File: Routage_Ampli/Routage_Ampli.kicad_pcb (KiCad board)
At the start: 2 copper layers, 3 parts

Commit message: Début Placement + Routage
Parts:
- removed REF**: PhoenixContact_MSTBVA_2,5_2-G-5,08_1x02_P5.08mm_Vertical, Connector_Phoenix_MSTB:PhoenixContact_MSTBVA_2,5_2-G-5,08_1x02_P5.08mm_Vertical
- removed REF**: PhoenixContact_MSTBVA_2,5_3-G-5,08_1x03_P5.08mm_Vertical, Connector_Phoenix_MSTB:PhoenixContact_MSTBVA_2,5_3-G-5,08_1x03_P5.08mm_Vertical
- removed REF**: Jack_35RAPC2AV, Routage_Ampli:Jack_35RAPC2AV
- added C1: 47µ, CmpAmpliAudio:CP_Radial_D8.0mm_P5.00mm, F.Cu at (110.5, 125.7)
- added C10: 470µ, CmpAmpliAudio:CP_Radial_D12.5mm_P5.00mm, F.Cu at (176.5, 61.0)
- added C11: 100n, CmpAmpliAudio:C_Rect_L7.2mm_W3.5mm_P5.00mm_FKS2_FKP2_MKS2_MKP2, F.Cu at (170.2, 49.5)
- added C2: C, CmpAmpliAudio:C_Rect_L7.2mm_W3.5mm_P5.00mm_FKS2_FKP2_MKS2_MKP2, F.Cu at (142.2, 99.1)
- added C3: 47µ, CmpAmpliAudio:CP_Radial_D8.0mm_P5.00mm, F.Cu at (152.4, 62.2)
- added C4: 10µ, CmpAmpliAudio:CP_Radial_D8.0mm_P5.00mm, F.Cu at (114.3, 57.1)
- added C5: 100n, CmpAmpliAudio:C_Rect_L7.2mm_W3.5mm_P5.00mm_FKS2_FKP2_MKS2_MKP2, F.Cu at (110.5, 68.6)
- added C6: 10µ, CmpAmpliAudio:CP_Radial_D8.0mm_P5.00mm, F.Cu at (157.5, 49.5)
- added C7: 100n, CmpAmpliAudio:C_Rect_L7.2mm_W3.5mm_P5.00mm_FKS2_FKP2_MKS2_MKP2, F.Cu at (146.1, 49.5)
- added C8: 470µ, CmpAmpliAudio:CP_Radial_D12.5mm_P5.00mm, F.Cu at (190.5, 71.1)
- added C9: 100n, CmpAmpliAudio:C_Rect_L7.2mm_W3.5mm_P5.00mm_FKS2_FKP2_MKS2_MKP2, F.Cu at (199.4, 64.8)
- added D1: 1N4148, CmpAmpliAudio:D_DO-35_SOD27_P10.16mm_Horizontal, F.Cu at (199.4, 69.8)
- added D2: 1N4148, CmpAmpliAudio:D_DO-35_SOD27_P10.16mm_Horizontal, F.Cu at (147.3, 61.0)
- added Dz1: BZX55C5V1, CmpAmpliAudio:D_DO-35_SOD27_P10.16mm_Horizontal, F.Cu at (138.4, 83.8)
- added HS1: Heatsink, CmpAmpliAudio:Heatsink_Fischer_SK104-STC-STIC_35x13mm_2xDrill2.5mm, F.Cu at (165.7, 130.8)
- added HS2: Heatsink, CmpAmpliAudio:Heatsink_Fischer_SK104-STC-STIC_35x13mm_2xDrill2.5mm, F.Cu at (137.8, 74.3)
- added J1: Conn_01x03, CmpAmpliAudio:PhoenixContact_MSTBVA_2,5_3-G-5,08_1x03_P5.08mm_Vertical, F.Cu at (133.3, 52.1)
- added J2: Conn_01x02, CmpAmpliAudio:PhoenixContact_MSTBVA_2,5_2-G-5,08_1x02_P5.08mm_Vertical, F.Cu at (186.7, 54.6)
- added Q1: 2N2907, CmpAmpliAudio:TO-18-3, F.Cu at (125.7, 109.2)
- added Q10: TIP32, CmpAmpliAudio:TO-220-3_Vertical, F.Cu at (140.3, 69.2)
- added Q11: BD138, CmpAmpliAudio:TO-126-3_Vertical, F.Cu at (168.9, 114.3)
- added Q12: TIP31, CmpAmpliAudio:TO-220-3_Vertical, F.Cu at (168.9, 125.7)
- added Q13: 2N2222, CmpAmpliAudio:TO-18-3, F.Cu at (185.4, 96.5)
- added Q2: 2N2907, CmpAmpliAudio:TO-18-3, F.Cu at (160.0, 109.2)
- added Q3: 2N2907, CmpAmpliAudio:TO-18-3, F.Cu at (115.6, 105.4)
- added Q4: 2N2222, CmpAmpliAudio:TO-18-3, F.Cu at (157.5, 101.6)
- added Q5: 2N2222, CmpAmpliAudio:TO-18-3, F.Cu at (162.6, 88.9)
- added Q6: 2N2907, CmpAmpliAudio:TO-18-3, F.Cu at (127.0, 85.1)
- added Q7: 2N2907, CmpAmpliAudio:TO-18-3, F.Cu at (127.0, 94.0)
- added Q8: BD139, CmpAmpliAudio:TO-126-3_Vertical, F.Cu at (149.9, 90.2)
- added Q9: BD139, CmpAmpliAudio:TO-126-3_Vertical, F.Cu at (162.6, 78.7)
- added R1: R, CmpAmpliAudio:R_Axial_DIN0207_L6.3mm_D2.5mm_P10.16mm_Horizontal, F.Cu at (116.8, 114.3)
- added R10: R, CmpAmpliAudio:R_Axial_DIN0207_L6.3mm_D2.5mm_P10.16mm_Horizontal, F.Cu at (134.6, 101.6)
- added R11: R, CmpAmpliAudio:R_Axial_DIN0516_L15.5mm_D5.0mm_P20.32mm_Horizontal, F.Cu at (200.7, 129.5)
- added R12: R, CmpAmpliAudio:R_Axial_DIN0516_L15.5mm_D5.0mm_P20.32mm_Horizontal, F.Cu at (193.0, 106.7)
- added R13: R, CmpAmpliAudio:R_Axial_DIN0207_L6.3mm_D2.5mm_P10.16mm_Horizontal, F.Cu at (188.0, 121.9)
- added R14: R, CmpAmpliAudio:R_Axial_DIN0207_L6.3mm_D2.5mm_P10.16mm_Horizontal, F.Cu at (143.5, 113.0)
- added R15: R, CmpAmpliAudio:R_Axial_DIN0207_L6.3mm_D2.5mm_P10.16mm_Horizontal, F.Cu at (148.6, 123.2)
- added R16: R, CmpAmpliAudio:R_Axial_DIN0207_L6.3mm_D2.5mm_P10.16mm_Horizontal, F.Cu at (119.4, 61.0)
- added R17: R, CmpAmpliAudio:R_Axial_DIN0207_L6.3mm_D2.5mm_P10.16mm_Horizontal, F.Cu at (184.2, 78.7)
- added R2: R, CmpAmpliAudio:R_Axial_DIN0207_L6.3mm_D2.5mm_P10.16mm_Horizontal, F.Cu at (175.3, 83.8)
- added R3: R, CmpAmpliAudio:R_Axial_DIN0207_L6.3mm_D2.5mm_P10.16mm_Horizontal, F.Cu at (180.3, 83.8)
- added R4: R, CmpAmpliAudio:R_Axial_DIN0207_L6.3mm_D2.5mm_P10.16mm_Horizontal, F.Cu at (134.6, 83.8)
- added R5: R, CmpAmpliAudio:R_Axial_DIN0207_L6.3mm_D2.5mm_P10.16mm_Horizontal, F.Cu at (116.8, 96.5)
- added R6: R, CmpAmpliAudio:R_Axial_DIN0207_L6.3mm_D2.5mm_P10.16mm_Horizontal, F.Cu at (170.2, 83.8)
- added R7: R, CmpAmpliAudio:R_Axial_DIN0207_L6.3mm_D2.5mm_P10.16mm_Horizontal, F.Cu at (108.0, 76.2)
- added R8: R, CmpAmpliAudio:R_Axial_DIN0207_L6.3mm_D2.5mm_P10.16mm_Horizontal, F.Cu at (152.4, 95.2)
- added R9: R, CmpAmpliAudio:R_Axial_DIN0207_L6.3mm_D2.5mm_P10.16mm_Horizontal, F.Cu at (108.0, 82.5)
- added RV1: R_POT, CmpAmpliAudio:Potentiometer_Bourns_3296W_Vertical, F.Cu at (143.5, 85.1)
- added RV2: R_POT, CmpAmpliAudio:Potentiometer_Bourns_3296W_Vertical, F.Cu at (115.6, 88.9)
- added U1: Jack_Mono, CmpAmpliAudio:Jack_35RAPC2AV, F.Cu at (132.1, 138.4)
- added U2: Relay_1CT, Routage_Ampli:Relay_CT, F.Cu at (201.9, 92.7)
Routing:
- net GND: track 0.00 -> 234.8 mm
- net +12V: track 0.00 -> 91.0 mm
- net -12V: track 0.00 -> 57.0 mm
- net Net-(Q10-Pad2): track 0.00 -> 35.7 mm
- net Net-(Q6-Pad3): track 0.00 -> 32.5 mm
- net Net-(C3-Pad1): track 0.00 -> 26.2 mm
- net Net-(Q10-Pad1): track 0.00 -> 25.6 mm
- net Net-(Q8-Pad3): track 0.00 -> 7.40 mm
- net Net-(R10-Pad2): track 0.00 -> 2.54 mm
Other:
- board outline added: 110.5 x 100.3 mm
- net class Default: clearance 0.2 -> 0.3; trace_width 0.25 -> 0.6; via_dia 0.8 -> 1.9; via_drill 0.4 -> 0.6
- rule trace_clearance: 0.2 -> 0.3
- rule trace_min: 0.2 -> 0.4
- rule via_min_drill: 0.3 -> 0.6
- rule via_min_size: 0.4 -> 0.6

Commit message: Version avant correction
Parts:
- moved HS2 70.0 mm to (194.3, 115.6), turned to 270 degrees
- moved HS1 68.4 mm to (134.6, 69.8)
- moved R3 67.1 mm to (127.0, 124.5), turned to 270 degrees
- moved R16 61.3 mm to (179.1, 74.9), turned to 90 degrees
- moved C11 61.0 mm to (167.6, 110.5)
- moved R2 58.4 mm to (133.3, 124.5), turned to 270 degrees
- moved C8 52.4 mm to (177.8, 121.9), turned to 0 degrees
- moved R11 50.8 mm to (160.0, 99.1)
- moved R15 50.3 mm to (184.2, 87.6), turned to 0 degrees
- moved R6 47.7 mm to (147.3, 125.7), turned to 270 degrees
- moved Q13 46.0 mm to (166.2, 54.7)
- moved R14 45.5 mm to (185.4, 95.2), turned to 0 degrees
- moved Q2 43.6 mm to (116.8, 115.6), turned to 0 degrees
- moved Q5 43.3 mm to (139.7, 125.7), turned to 0 degrees
- moved D1 42.8 mm to (157.5, 61.0), turned to 90 degrees
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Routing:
- net -12V: track 57.0 -> 320.1 mm
- net GND: track 234.8 -> 0.00 mm
- net +12V: track 91.0 -> 174.5 mm
- net Net-(Q10-Pad2): track 35.7 -> 0.00 mm
- net Net-(Q6-Pad3): track 32.5 -> 0.00 mm
- net Net-(C3-Pad1): track 26.2 -> 0.00 mm
- net Net-(Q10-Pad1): track 25.6 -> 0.00 mm
- net Net-(Q8-Pad3): track 7.40 -> 0.00 mm
- net Net-(C2-Pad1): track 0.00 -> 4.22 mm
- net Net-(R10-Pad2): track 2.54 -> 0.00 mm
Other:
- outline, holes or cut-outs redrawn
- board text added: "CROUARD - HATIBI 3 IMACS AE - 2021"

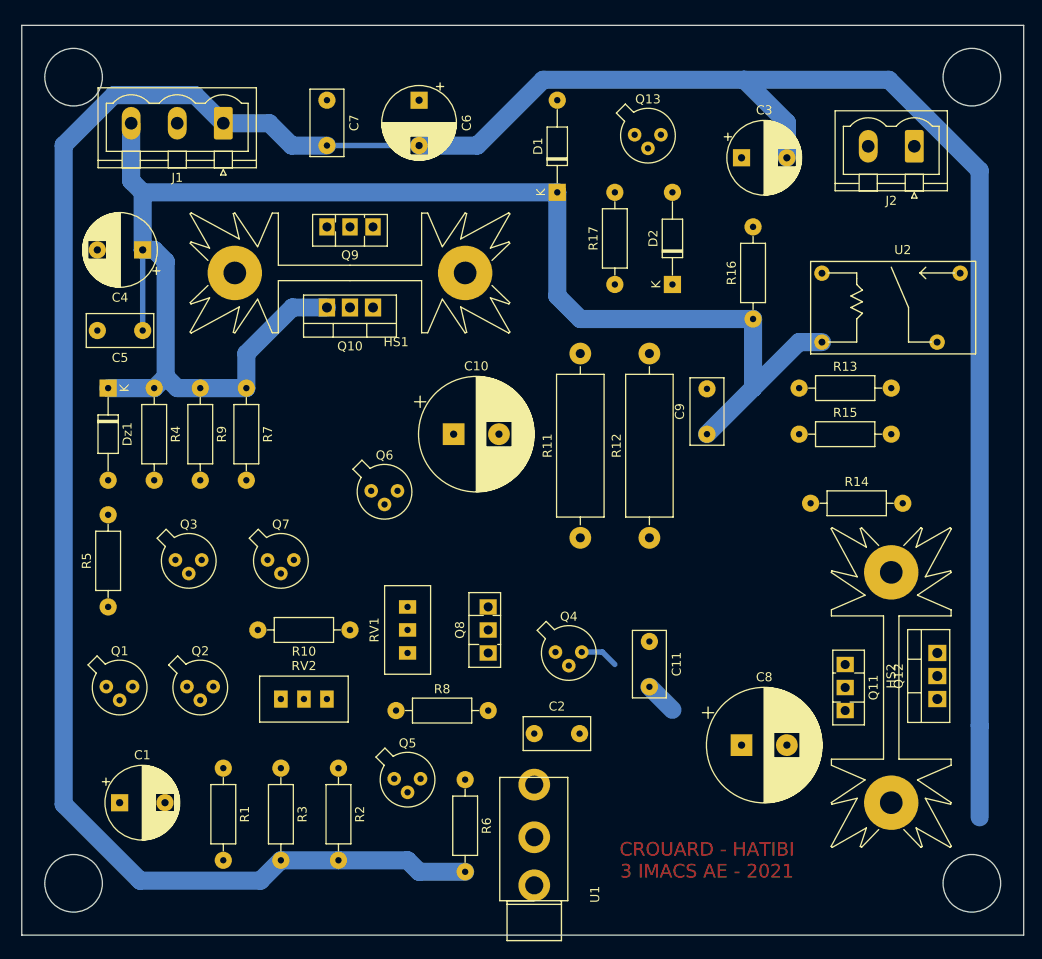
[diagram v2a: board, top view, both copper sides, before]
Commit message: Version pour correction : J-7
Le plan de masse n'a pas été réalisé. On a routé les GND ensemble plutôt. On attend le Go de Mr Rocacher pour le faire.

Le DRC fonctionne mais pas sûrs que les largeurs soient bonnes ni qu'il y ait des fils trop longs.
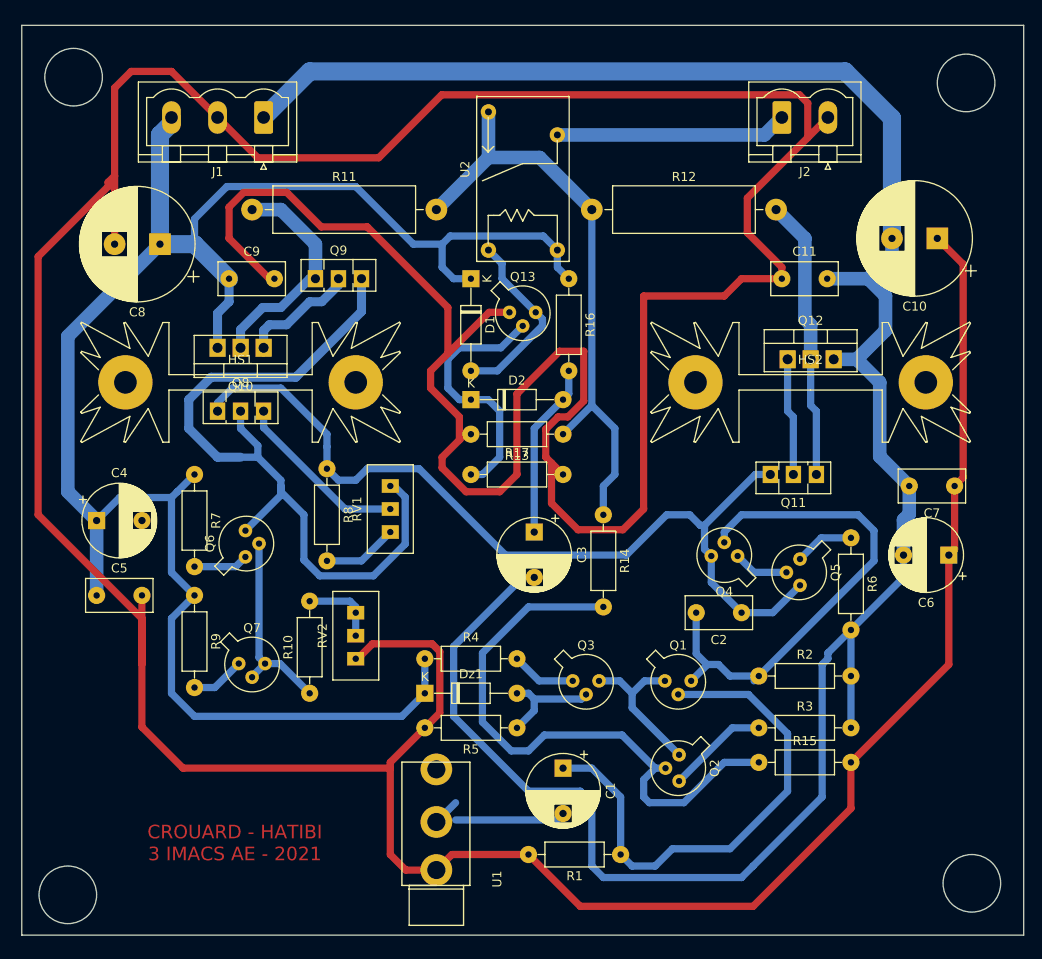
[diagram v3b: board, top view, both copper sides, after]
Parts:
- moved C8 84.6 mm to (113.7, 66.7), turned to 180 degrees
- moved C7 81.2 mm to (201.3, 93.3), turned to 180 degrees
- moved C6 77.0 mm to (200.7, 101.0), turned to 180 degrees
- moved Q1 61.6 mm to (169.5, 114.9)
- moved C10 57.5 mm to (199.4, 66.0), turned to 180 degrees
- moved C9 55.4 mm to (121.3, 70.5), turned to 0 degrees
- moved Q2 54.5 mm to (170.8, 123.2), turned to 270 degrees
- moved R3 52.9 mm to (179.7, 120.0), turned to 0 degrees
- moved R11 51.2 mm to (123.8, 62.9), turned to 0 degrees
- moved Q5 50.6 mm to (184.2, 101.6), turned to 270 degrees
- moved R6 50.2 mm to (189.9, 99.1)
- moved C1 49.0 mm to (158.1, 124.5), turned to 270 degrees
- moved Dz1 48.5 mm to (142.9, 116.2), turned to 0 degrees
- moved U2 47.6 mm to (147.3, 59.7), turned to 90 degrees
- moved R2 47.5 mm to (179.7, 114.3), turned to 0 degrees
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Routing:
- net GND: track 0.00 -> 570.0 mm
- net Net-(C2-Pad1): track 4.22 -> 97.6 mm
- net Net-(Q6-Pad3): track 0.00 -> 85.3 mm
- net -12V: track 320.1 -> 250.1 mm
- net Net-(R11-Pad2): track 0.00 -> 66.7 mm
- net Net-(Q2-Pad2): track 0.00 -> 65.3 mm
- net Net-(C1-Pad1): track 0.00 -> 56.6 mm
- net Net-(C2-Pad2): track 0.00 -> 56.2 mm
- net Net-(Q11-Pad1): track 0.00 -> 31.1 mm
- net +12V: track 174.5 -> 204.4 mm
- net Net-(D2-Pad1): track 0.00 -> 28.8 mm
- net Net-(J2-Pad1): track 0.00 -> 25.6 mm
- net Net-(Q10-Pad2): track 0.00 -> 25.0 mm
- net Net-(Q6-Pad2): track 0.00 -> 21.9 mm
- net Net-(D1-Pad2): track 0.00 -> 20.8 mm
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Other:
- outline, holes or cut-outs redrawn

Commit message: Version finale
Ajout u plan de masse et corrections des dernières erreurs. Sans straps en simple face. GG !
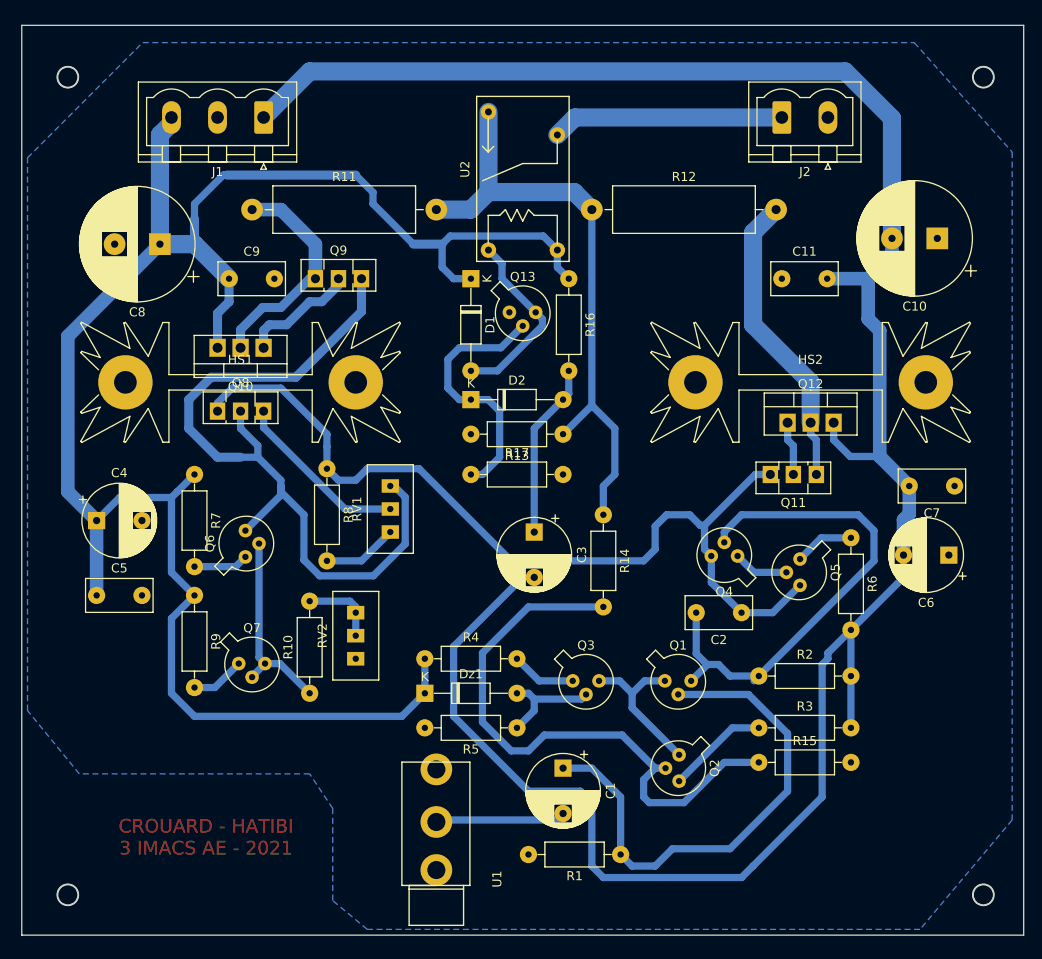
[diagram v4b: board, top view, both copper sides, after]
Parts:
- moved Q12 6.98 mm to (182.9, 86.4)
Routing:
- net GND: track 570.0 -> 0.00 mm
- net Net-(Q11-Pad2): track 13.0 -> 5.98 mm
- net -12V: track 250.1 -> 253.9 mm
- net +12V: track 204.4 -> 207.2 mm
- net Net-(Q11-Pad1): track 31.1 -> 33.2 mm
- net Net-(C2-Pad1): track 97.6 -> 99.7 mm
- net Net-(C1-Pad2): track 15.1 -> 14.4 mm
- net Net-(R11-Pad2): track 66.7 -> 67.3 mm
- net (no net): vias 0 -> 4
- added copper zone on B.Cu, net GND
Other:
- outline, holes or cut-outs redrawn

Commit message: Derniers détails
Ajout de derniers détails : Texte en bottom, diodes de protection, mise à jour de la lib
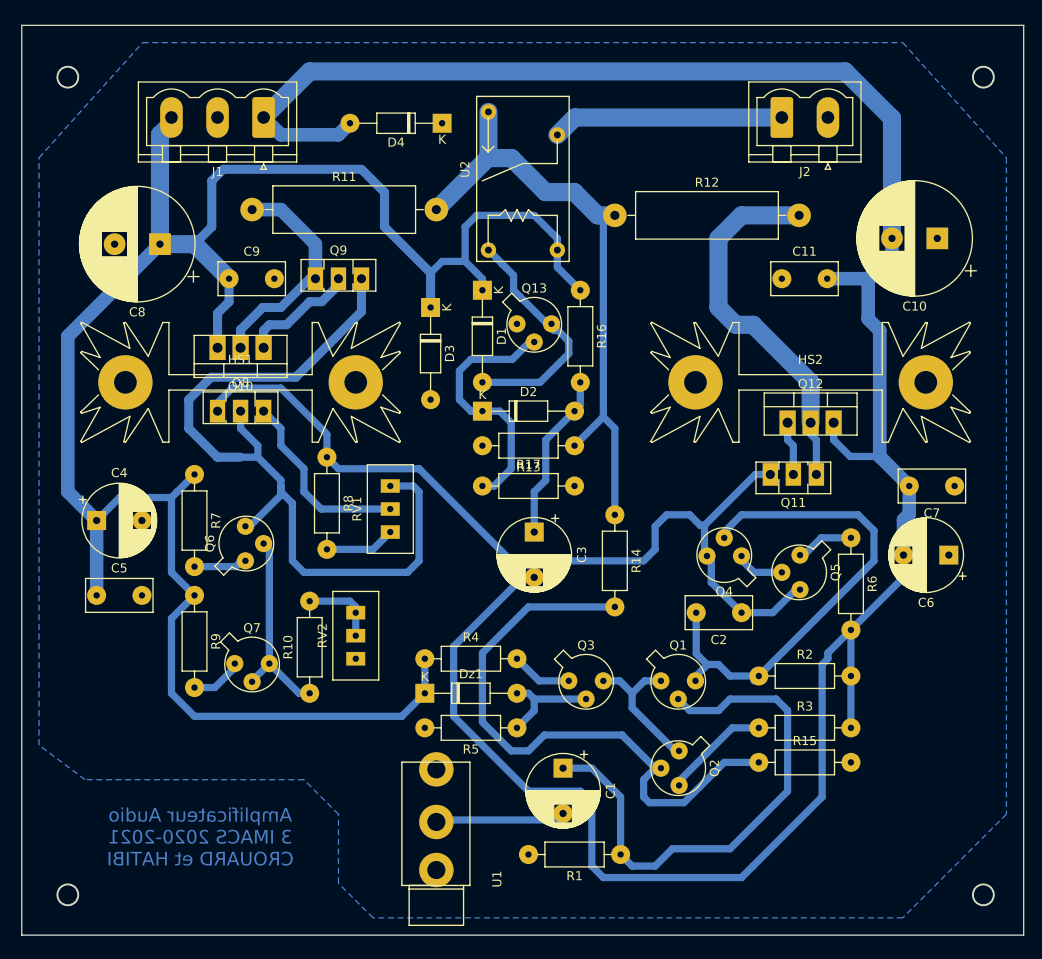
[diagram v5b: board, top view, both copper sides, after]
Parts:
- added D3: 1N4001, CmpAmpliAudio:D_DO-35_SOD27_P10.16mm_Horizontal, F.Cu at (143.5, 73.7)
- added D4: 1N4001, CmpAmpliAudio:D_DO-35_SOD27_P10.16mm_Horizontal, F.Cu at (144.8, 53.3)
- moved R12 2.62 mm to (163.8, 63.5)
- moved R16 1.80 mm to (160.0, 71.8)
- moved D2 1.80 mm to (149.2, 85.1)
- moved R13 1.80 mm to (159.4, 88.9)
- moved D1 1.80 mm to (149.2, 71.8)
- moved Q13 1.80 mm to (153.7, 75.6)
- moved R17 1.80 mm to (149.2, 93.3)
- moved R14 1.27 mm to (163.8, 96.5)
- moved R8 1.27 mm to (132.1, 90.2)
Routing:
- net +12V: track 207.2 -> 220.4 mm
- net -12V: track 253.9 -> 264.8 mm
- net Net-(Q11-Pad1): track 33.2 -> 41.6 mm
- net Net-(D1-Pad2): track 20.8 -> 26.8 mm
- net Net-(Q6-Pad3): track 85.3 -> 90.7 mm
- net Net-(C1-Pad1): track 56.6 -> 58.9 mm
- net Net-(C2-Pad1): track 99.7 -> 97.8 mm
- net Net-(Q8-Pad3): track 19.5 -> 21.0 mm
- net Net-(Q2-Pad2): track 65.3 -> 66.6 mm
- net Net-(C3-Pad1): track 19.4 -> 18.6 mm
- net Net-(R8-Pad2): track 8.30 -> 7.77 mm
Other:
- board text added: "Amplificateur Audio 3 IMACS 2020-2021 CROUARD et HATIBI"
- board text removed: "CROUARD - HATIBI 3 IMACS AE - 2021"
